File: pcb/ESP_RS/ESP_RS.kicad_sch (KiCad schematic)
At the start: 51 parts, among them J1 Conn_01x02, J2 USB_C_Receptacle_USB2.0_16P, J3 Conn_01x07_Socket, J4 Conn_02x05_Counter_Clockwise, Q1 SS8050, Q2 SS8050, U1 AMS1117-3.3, U2 TPS54202DDC, U3 CP2102N-Axx-xQFN28, U4 ESP32-WROOM-32E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

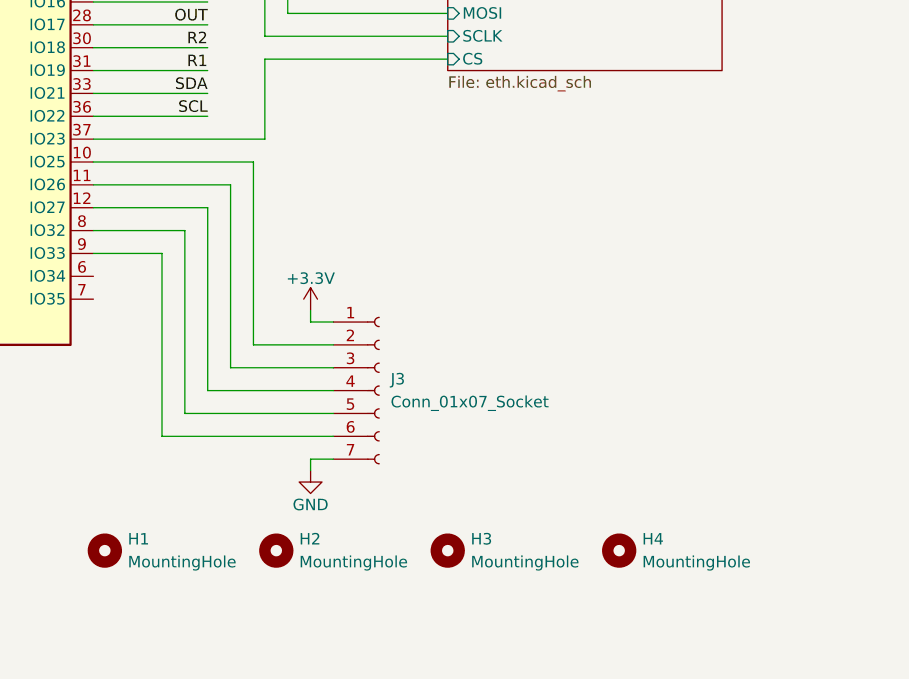
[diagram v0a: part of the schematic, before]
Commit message: Add ADC battery sampling
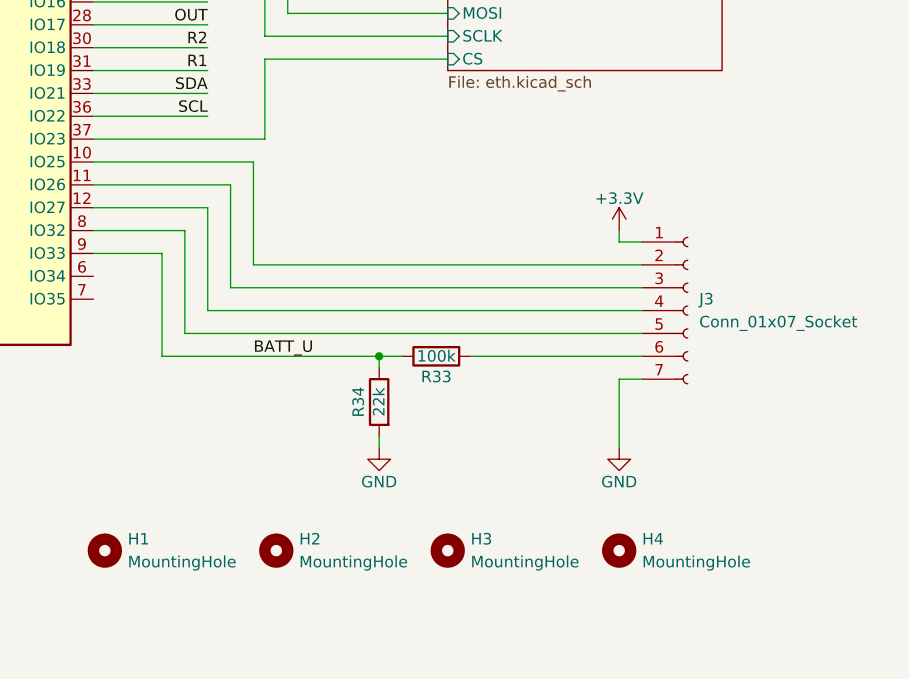
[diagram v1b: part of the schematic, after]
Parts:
- added R33: 100k, Resistor_SMD:R_0603_1608Metric, symbol Device:R
- added R34: 22k, Resistor_SMD:R_0603_1608Metric, symbol Device:R
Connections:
- net GND: now also R34.2
- net at J3.6 (Pin_6): now also R33.2; no longer U4.9 (IO33)
- new net BATT_U: R33.1, R34.1, U4.9 (IO33)
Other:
- moved on the sheet: J3

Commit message: v
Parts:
- removed J3: Conn_01x07_Socket, Connector_JST:JST_XH_B7B-XH-A_1x07_P2.50mm_Vertical, symbol Connector:Conn_01x07_Socket
- removed J4: Conn_02x05_Counter_Clockwise, Connector_IDC:IDC-Header_2x05_P2.54mm_Horizontal, symbol Connector_Generic:Conn_02x05_Counter_Clockwise
- removed JP1: 5V_EN, TestPoint:TestPoint_2Pads_Pitch2.54mm_Drill0.8mm, symbol Jumper:Jumper_2_Open
- removed R16: 2k1, Resistor_SMD:R_0603_1608Metric, symbol Device:R
- removed R33: 100k, Resistor_SMD:R_0603_1608Metric, symbol Device:R
- removed R34: 22k, Resistor_SMD:R_0603_1608Metric, symbol Device:R
- removed U5: 74LVC1G17, Package_TO_SOT_SMD:SOT-23-5, symbol 74xGxx:74LVC1G17
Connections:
- net SCL is gone; now on net TX: U4.36 (IO22)
- net SDA is gone; now on net RX: U4.33 (IO21)
- net BATT_U: no longer names the net of U4.9 (IO33)
- net OUT renamed RE/DE
- net R1: no longer names the net of U4.31 (IO19)
- net R2: no longer names the net of U4.30 (IO18)
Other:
- added sheet RS485 (rs485.kicad_sch)
